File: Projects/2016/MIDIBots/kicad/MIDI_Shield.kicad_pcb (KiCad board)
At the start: 2 copper layers, 86.4 x 77.5 mm, 71 parts, among them IC1 PC900V, K1 SRVO1, K2 SRVO2, K3 SRVO3, P10 A3, P11 A4, P12 AUX_12V, P13 AUX_12V, P14 AUX_5V, P15 AUX_5V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

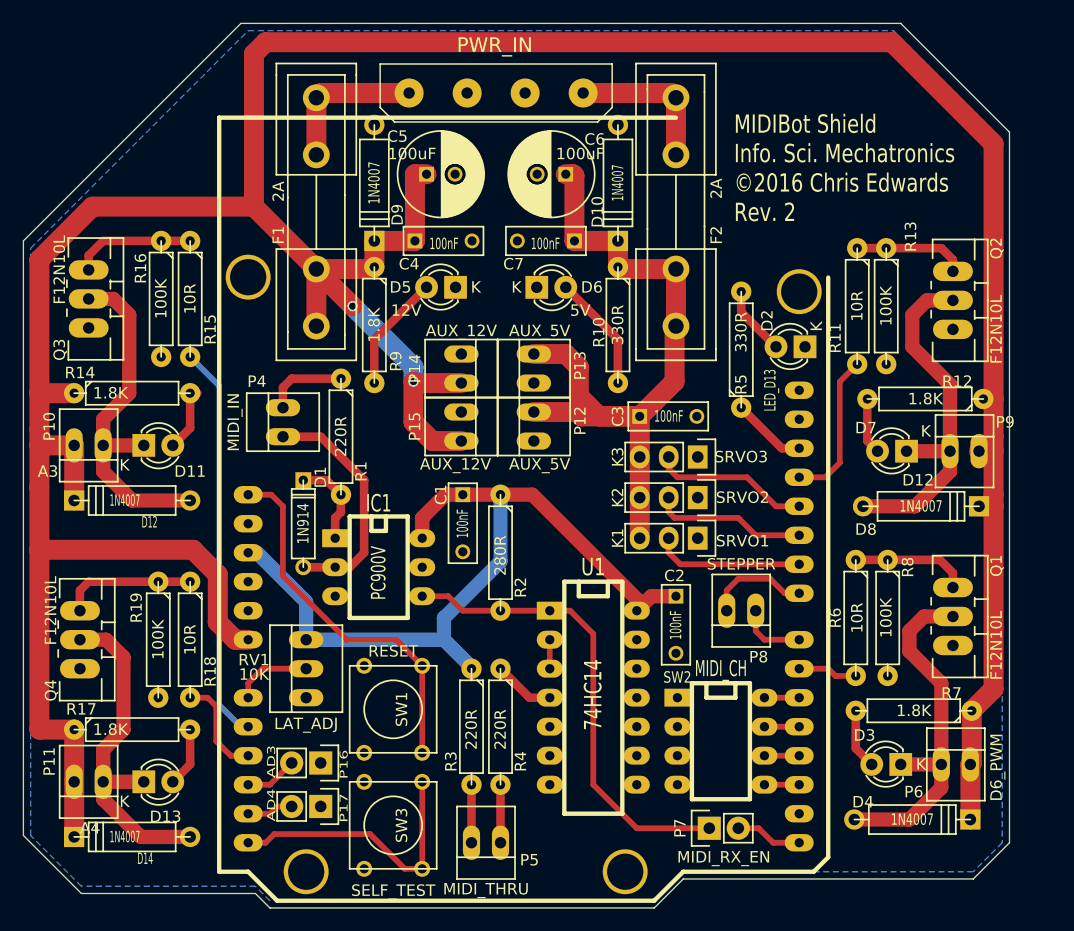
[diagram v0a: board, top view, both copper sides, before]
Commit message: [Y] Make MOSFET connector labels more consistent.
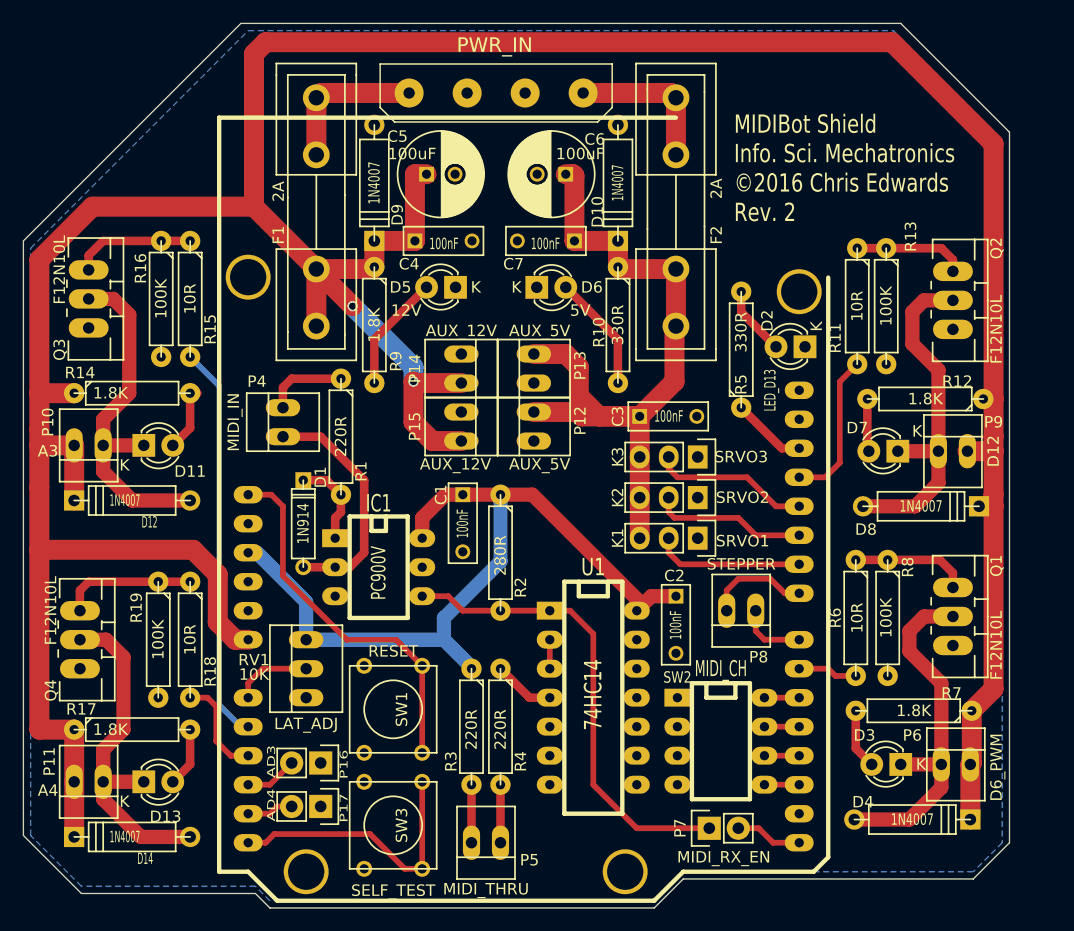
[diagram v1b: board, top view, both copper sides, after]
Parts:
- moved P9 1.02 mm to (135.4, 110.5)
- moved D7 0.76 mm to (130.6, 110.5)
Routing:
- net +12V: track 311.6 -> 312.6 mm
- net Net-(D7-Pad1): track 31.9 -> 30.9 mm
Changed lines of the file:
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@@
   (layers
     (0 F.Cu signal)
-    (31 B.Cu signal)
+    (31 B.Cu signal hide)
     (32 B.Adhes user)
     (33 F.Adhes user)
@@
   )
   (module LEDs:LED-3MM (layer F.Cu)
-    (at 131.318 110.49 180)
+    (at 130.556 110.49 180)
     (descr "LED 3mm round vertical")
     (tags "LED  3mm round vertical")
@@
     (at 135.636 137.922)
     (attr virtual)
-    (fp_text reference P6 (at -3.683 2.413) (layer F.SilkS)
+    (fp_text reference P6 (at -3.81 -2.54) (layer F.SilkS)
       (effects (font (size 1 1) (thickness 0.15)))
     )
@@
   )
   (module Connect:PINHEAD1-2 (layer F.Cu)
-    (at 136.398 110.49)
+    (at 135.382 110.49)
     (attr virtual)
     (fp_text reference P9 (at 3.556 -2.54) (layer F.SilkS)
       (effects (font (size 1 1) (thickness 0.15)))
     )
-    (fp_text value D12 (at -4.064 2.54 180) (layer F.SilkS)
+    (fp_text value D12 (at 3.556 0 270) (layer F.SilkS)
       (effects (font (size 1 1) (thickness 0.15)))
     )
@@
     (at 59.69 109.982 180)
     (attr virtual)
-    (fp_text reference P10 (at 3.429 1.651 270) (layer F.SilkS)
-      (effects (font (size 1 1) (thickness 0.15)))
-    )
-    (fp_text value A3 (at 3.556 -2.286 180) (layer F.SilkS)
+    (fp_text reference P10 (at 3.556 2.032 270) (layer F.SilkS)
+      (effects (font (size 1 1) (thickness 0.15)))
+    )
+    (fp_text value A3 (at 3.556 -0.508 180) (layer F.SilkS)
       (effects (font (size 1 1) (thickness 0.15)))
     )
@@
       (effects (font (size 1 1) (thickness 0.15)))
     )
-    (fp_text value A4 (at -0.127 -4.064 180) (layer F.SilkS)
+    (fp_text value A4 (at 3.556 -0.762 180) (layer F.SilkS)
       (effects (font (size 1 1) (thickness 0.15)))
     )
@@
   (segment (start 131.572 142.748) (end 126.746 142.748) (width 1.25) (layer F.Cu) (net 24))
   (segment (start 134.366 139.954) (end 131.572 142.748) (width 1.25) (layer F.Cu) (net 24))
+  (segment (start 136.652 110.49) (end 138.938 110.49) (width 1.75) (layer F.Cu) (net 25))
   (segment (start 137.668 115.316) (end 138.938 115.316) (width 1.75) (layer F.Cu) (net 25))
-  (segment (start 137.668 110.49) (end 138.938 110.49) (width 1.75) (layer F.Cu) (net 25))
   (segment (start 58.42 139.446) (end 58.42 134.874) (width 1.75) (layer F.Cu) (net 25))
   (segment (start 58.42 144.272) (end 58.42 139.446) (width 1.75) (layer F.Cu) (net 25))
@@
   (segment (start 118.364 143.51) (end 116.586 143.51) (width 0.5) (layer F.Cu) (net 27))
   (segment (start 119.634 144.78) (end 118.364 143.51) (width 0.5) (layer F.Cu) (net 27))
-  (segment (start 135.128 110.49) (end 135.128 112.268) (width 1.25) (layer F.Cu) (net 28))
+  (segment (start 134.112 110.49) (end 134.112 103.378) (width 1.25) (layer F.Cu) (net 28))
+  (segment (start 132.842 97.282) (end 135.382 97.282) (width 1.25) (layer F.Cu) (net 28))
+  (segment (start 131.826 98.298) (end 132.842 97.282) (width 1.25) (layer F.Cu) (net 28))
+  (segment (start 131.826 101.092) (end 131.826 98.298) (width 1.25) (layer F.Cu) (net 28))
+  (segment (start 134.112 103.378) (end 131.826 101.092) (width 1.25) (layer F.Cu) (net 28))
+  (segment (start 130.556 110.49) (end 134.112 110.49) (width 1.25) (layer F.Cu) (net 28))
+  (segment (start 134.112 110.49) (end 134.112 113.284) (width 1.25) (layer F.Cu) (net 28))
   (segment (start 132.08 115.316) (end 127.508 115.316) (width 1.25) (layer F.Cu) (net 28))
-  (segment (start 135.128 112.268) (end 132.08 115.316) (width 1.25) (layer F.Cu) (net 28))
-  (segment (start 135.128 110.49) (end 135.128 104.648) (width 1.25) (layer F.Cu) (net 28))
-  (segment (start 133.096 97.282) (end 135.382 97.282) (width 1.25) (layer F.Cu) (net 28))
-  (segment (start 131.826 98.552) (end 133.096 97.282) (width 1.25) (layer F.Cu) (net 28))
-  (segment (start 131.826 101.346) (end 131.826 98.552) (width 1.25) (layer F.Cu) (net 28))
-  (segment (start 135.128 104.648) (end 131.826 101.346) (width 1.25) (layer F.Cu) (net 28))
-  (segment (start 131.318 110.49) (end 135.128 110.49) (width 1.25) (layer F.Cu) (net 28))
-  (segment (start 127.889 105.918) (end 127.889 109.601) (width 0.75) (layer F.Cu) (net 29))
-  (segment (start 127.889 109.601) (end 128.778 110.49) (width 0.75) (layer F.Cu) (net 29))
+  (segment (start 134.112 113.284) (end 132.08 115.316) (width 1.25) (layer F.Cu) (net 28))
+  (segment (start 127.889 105.918) (end 127.889 110.363) (width 0.75) (layer F.Cu) (net 29))
+  (segment (start 127.889 110.363) (end 128.016 110.49) (width 0.75) (layer F.Cu) (net 29))
   (segment (start 129.54 92.71) (end 134.366 92.71) (width 0.75) (layer F.Cu) (net 30))
   (segment (start 135.382 93.726) (end 135.382 94.742) (width 0.75) (layer F.Cu) (net 30))
@@
   (segment (start 124.46 129.54) (end 125.095 130.175) (width 0.5) (layer F.Cu) (net 44))
   (segment (start 121.92 112.776) (end 124.206 112.776) (width 0.5) (layer F.Cu) (net 45))
+  (segment (start 124.206 112.776) (end 125.476 111.506) (width 0.5) (layer F.Cu) (net 45))
+  (segment (start 125.476 111.506) (end 125.476 104.394) (width 0.5) (layer F.Cu) (net 45))
   (segment (start 125.476 104.394) (end 127 102.87) (width 0.5) (layer F.Cu) (net 45))
-  (segment (start 125.476 111.506) (end 125.476 104.394) (width 0.5) (layer F.Cu) (net 45))
-  (segment (start 124.206 112.776) (end 125.476 111.506) (width 0.5) (layer F.Cu) (net 45))
   (segment (start 73.66 134.62) (end 73.025 134.62) (width 0.5) (layer B.Cu) (net 46))
   (segment (start 73.025 134.62) (end 71.12 132.715) (width 0.5) (layer B.Cu) (net 46))

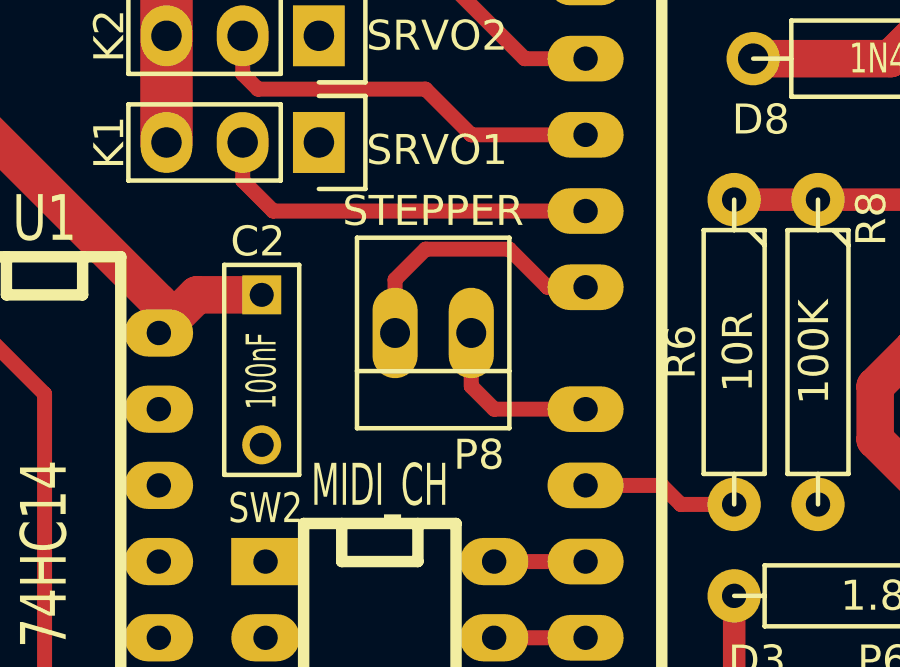
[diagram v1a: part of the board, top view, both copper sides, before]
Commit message: Reoriented stepper step/dir header
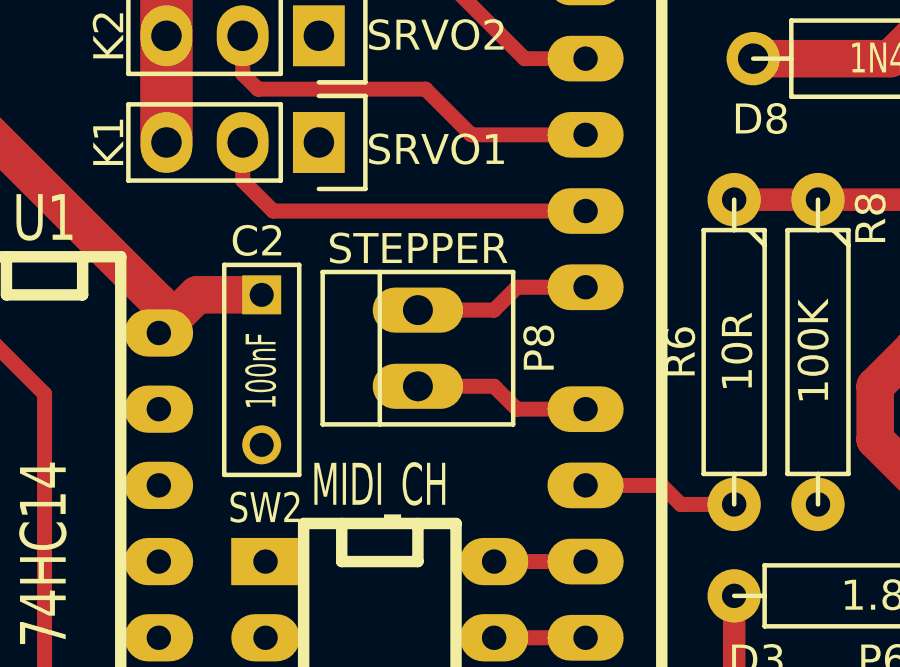
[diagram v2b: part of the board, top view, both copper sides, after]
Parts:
- moved P8 0.72 mm to (116.3, 125.0), turned to 90 degrees
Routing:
- net /STEPPER_STEP: track 9.07 -> 5.90 mm
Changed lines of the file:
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@@
     (links 151)
     (no_connects 0)
-    (area 53.924999 72.974999 140.385001 150.545001)
+    (area 49.899999 59.899999 150.100001 160.100001)
     (thickness 1.6)
     (drawings 18)
-    (tracks 263)
+    (tracks 261)
     (zones 0)
     (modules 71)
@@
   )
   (module Connect:PINHEAD1-2 (layer F.Cu)
-    (at 116.84 124.46 180)
+    (at 116.332 124.968 90)
     (attr virtual)
-    (fp_text reference P8 (at -1.524 -4.064 180) (layer F.SilkS)
-      (effects (font (size 1 1) (thickness 0.15)))
-    )
-    (fp_text value STEPPER (at 0 4.064 180) (layer F.SilkS)
+    (fp_text reference P8 (at 0 4.064 270) (layer F.SilkS)
+      (effects (font (size 1 1) (thickness 0.15)))
+    )
+    (fp_text value STEPPER (at 3.302 0 180) (layer F.SilkS)
       (effects (font (size 1 1) (thickness 0.15)))
     )
@@
     (fp_line (start -2.54 -3.175) (end -2.54 3.175) (layer F.SilkS) (width 0.15))
     (fp_line (start 2.54 -3.175) (end 2.54 3.175) (layer F.SilkS) (width 0.15))
-    (pad 1 thru_hole oval (at -1.27 0 180) (size 1.50622 3.01498) (drill 0.99822) (layers *.Cu *.Mask)
+    (pad 1 thru_hole oval (at -1.27 0 90) (size 1.50622 3.01498) (drill 0.99822) (layers *.Cu *.Mask)
       (net 17 /STEPPER_DIR))
-    (pad 2 thru_hole oval (at 1.27 0 180) (size 1.50622 3.01498) (drill 0.99822) (layers *.Cu *.Mask)
+    (pad 2 thru_hole oval (at 1.27 0 90) (size 1.50622 3.01498) (drill 0.99822) (layers *.Cu *.Mask)
       (net 18 /STEPPER_STEP))
   )
@@
   (segment (start 73.66 130.81) (end 73.66 132.08) (width 0.5) (layer F.Cu) (net 16))
   (segment (start 74.93 129.54) (end 73.66 130.81) (width 0.5) (layer F.Cu) (net 16))
-  (segment (start 121.92 127) (end 118.872 127) (width 0.5) (layer F.Cu) (net 17))
-  (segment (start 118.11 126.238) (end 118.11 124.46) (width 0.5) (layer F.Cu) (net 17))
-  (segment (start 118.872 127) (end 118.11 126.238) (width 0.5) (layer F.Cu) (net 17))
-  (segment (start 121.92 122.936) (end 120.65 122.936) (width 0.5) (layer F.Cu) (net 18))
-  (segment (start 120.65 122.936) (end 119.38 121.666) (width 0.5) (layer F.Cu) (net 18))
-  (segment (start 119.38 121.666) (end 116.586 121.666) (width 0.5) (layer F.Cu) (net 18))
-  (segment (start 116.586 121.666) (end 115.57 122.682) (width 0.5) (layer F.Cu) (net 18))
-  (segment (start 115.57 122.682) (end 115.57 124.46) (width 0.5) (layer F.Cu) (net 18))
+  (segment (start 121.92 127) (end 119.634 127) (width 0.5) (layer F.Cu) (net 17) (status 400000))
+  (segment (start 118.872 126.238) (end 116.332 126.238) (width 0.5) (layer F.Cu) (net 17) (status 800000))
+  (segment (start 119.634 127) (end 118.872 126.238) (width 0.5) (layer F.Cu) (net 17))
+  (segment (start 121.92 122.936) (end 119.634 122.936) (width 0.5) (layer F.Cu) (net 18) (status 400000))
+  (segment (start 118.872 123.698) (end 116.332 123.698) (width 0.5) (layer F.Cu) (net 18) (status 800000))
+  (segment (start 119.634 122.936) (end 118.872 123.698) (width 0.5) (layer F.Cu) (net 18))
   (segment (start 121.92 120.396) (end 111.506 120.396) (width 0.5) (layer F.Cu) (net 19))
   (segment (start 110.49 119.38) (end 110.49 118.11) (width 0.5) (layer F.Cu) (net 19))
